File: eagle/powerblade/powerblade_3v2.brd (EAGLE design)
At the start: 25.4 x 25.4 mm, 80 parts, among them J1 JTAG_14PIN_IDC-ND, J2 AC_INF2, J4 TC2030-JLINK-NL, Q1 NTS4173, Q4 2SK1829, U1 TPS62122, U2 MCP6V3, U3 MSP430FR5738, U4 NRF51822QF, U6 MAX9910, U7 OPA2369, X1 16MHz, X3 32.768kHz, Y1 UREACH_XTEND

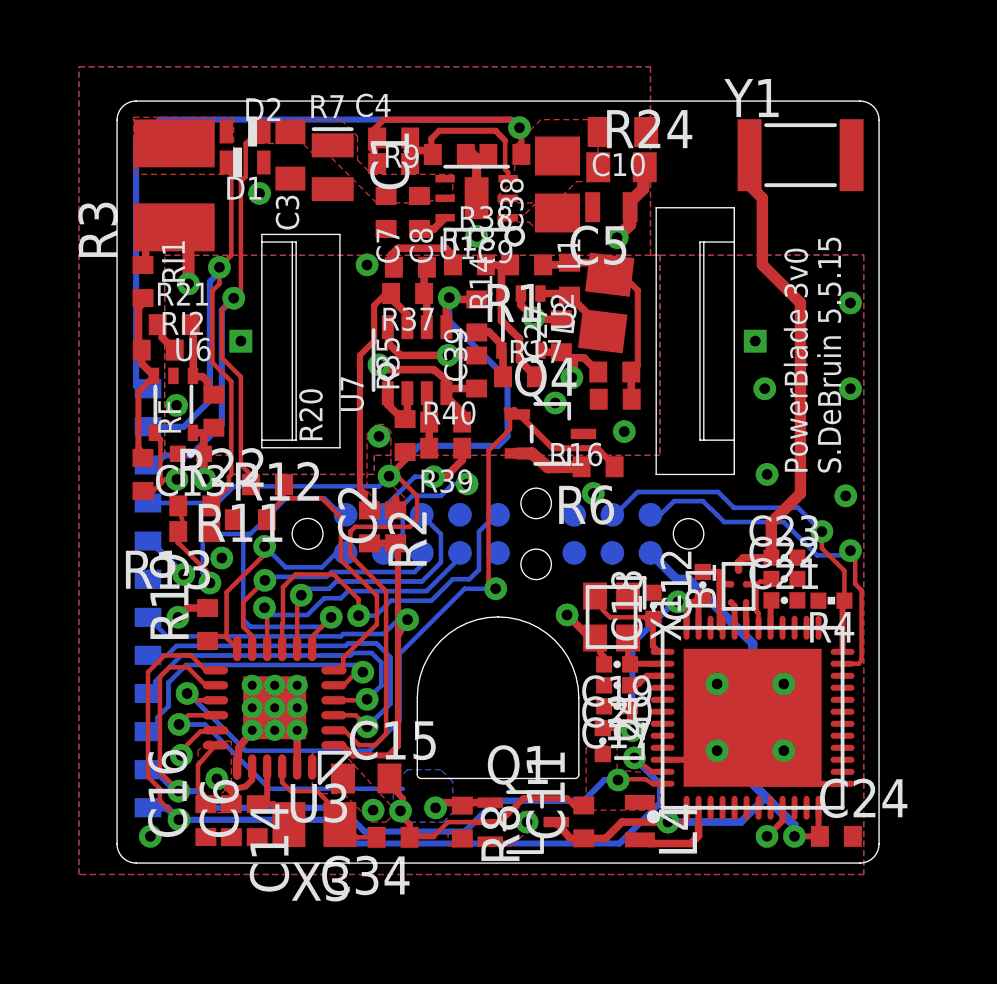
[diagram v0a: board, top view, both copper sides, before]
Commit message: updated powerblade 3v2 to include AC_F3
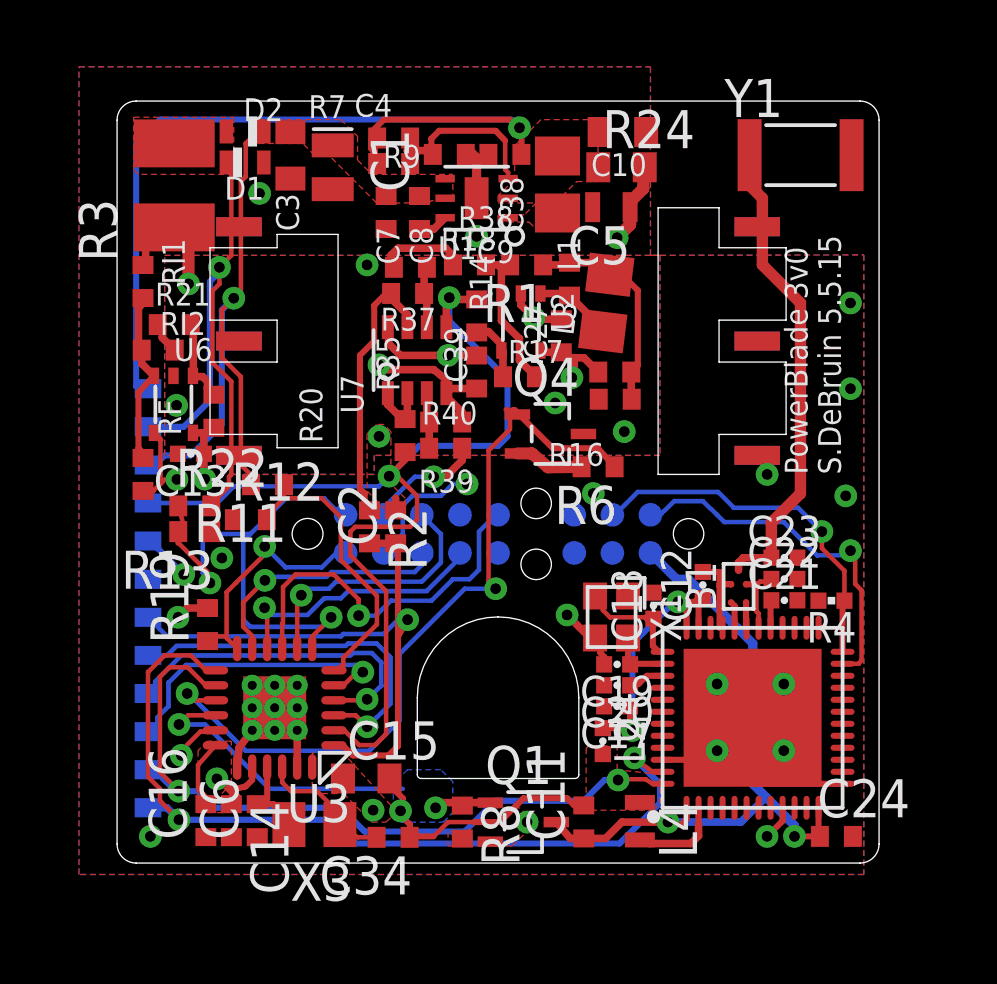
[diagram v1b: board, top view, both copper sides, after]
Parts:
- J2: value AC_INF2 -> AC_INF3; device powerfilm:AC3_F2 -> powerfilm:AC3_F3
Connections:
- net GND: now also J2.PB.1, J2.PB.2, J2.PB.3, J2.PB.4, J2.PB.5, J2.PB.6; no longer J2.P2A
- net VTEST: now also J2.PA.1, J2.PA.2, J2.PA.3, J2.PA.4, J2.PA.5, J2.PA.6; no longer J2.P1A
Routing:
- net VTEST: track 7.21 -> 10.4 mm
- net GND: vias 17 -> 16
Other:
- outline, holes or cut-outs redrawn
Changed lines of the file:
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@@
 <attribute name="DIGIKEY" value="490-4025-1-ND" x="4.727575" y="-16.002" size="1.778" layer="27" rot="R270" display="off"/>
 </element>
-<element name="J2" library="powerfilm" package="AC3_F2" value="AC_INF2" x="0" y="0">
+<element name="J2" library="powerfilm" package="AC3_F3" value="AC_INF3" x="0" y="0">
 <attribute name="DIGIKEY" value="NP" x="0" y="0" size="1.778" layer="27" display="off"/>
 </element>
@@
 <contactref element="RI1" pad="1"/>
 <contactref element="R3" pad="1"/>
-<contactref element="J2" pad="P1A"/>
+<contactref element="J2" pad="PA.1"/>
 <via x="-10.31875" y="1.905" extent="1-16" drill="0.3556"/>
 <wire x1="-10.31875" y1="1.905" x2="-10.31875" y2="3.314875" width="0.4064" layer="1"/>
@@
 <wire x1="-10.31875" y1="1.905" x2="-10.31875" y2="1.031875" width="1.27" layer="2"/>
 <wire x1="-10.31875" y1="1.031875" x2="-9.286875" y2="0" width="1.27" layer="2"/>
-<wire x1="-9.286875" y1="0" x2="-8.5725" y2="0" width="1.27" layer="2"/>
+<wire x1="-9.286875" y1="0" x2="-8.636" y2="3.81" width="1.27" layer="2"/>
 <wire x1="-11.8364" y1="2.534375" x2="-11.7475" y2="2.623275" width="0.254" layer="1"/>
 <wire x1="-11.7475" y1="2.623275" x2="-11.7475" y2="3.4925" width="0.254" layer="1"/>
 <wire x1="-11.7475" y1="3.4925" x2="-11.448875" y2="3.791125" width="0.254" layer="1"/>
 <wire x1="-11.448875" y1="3.791125" x2="-10.795" y2="3.791125" width="0.254" layer="1"/>
+<contactref element="J2" pad="PA.2"/>
+<contactref element="J2" pad="PA.3"/>
+<contactref element="J2" pad="PA.4"/>
+<contactref element="J2" pad="PA.5"/>
+<contactref element="J2" pad="PA.6"/>
+<wire x1="-8.636" y1="-3.81" x2="-8.636" y2="-3.81" width="0" layer="19" extent="1-16"/>
+<wire x1="-8.636" y1="0" x2="-8.636" y2="-3.81" width="0" layer="19" extent="1-1"/>
+<wire x1="-8.636" y1="0" x2="-8.636" y2="0" width="0" layer="19" extent="1-16"/>
+<wire x1="-9.286875" y1="0" x2="-8.636" y2="0" width="0" layer="19" extent="1-2"/>
+<wire x1="-8.636" y1="3.81" x2="-8.636" y2="3.81" width="0" layer="19" extent="1-2"/>
+<wire x1="-8.636" y1="3.81" x2="-8.636" y2="3.81" width="0" layer="19" extent="2-16"/>
 </signal>
 <signal name="VAMP">
@@
 <via x="-9.2075" y="-7.23138125" extent="1-16" drill="0.3556"/>
 <via x="-11.58875" y="-16.51" extent="1-16" drill="0.3556"/>
-<contactref element="J2" pad="P2A"/>
+<contactref element="J2" pad="PB.1"/>
 <wire x1="-3.81" y1="-7.0612" x2="-3.806825" y2="-7.0612" width="0.1524" layer="16"/>
 <wire x1="-3.806825" y1="-7.0612" x2="-3.175" y2="-6.429375" width="0.1524" layer="16"/>
@@
 <wire x1="-1.508125" y1="-4.7625" x2="-1.031875" y2="-4.7625" width="0.1524" layer="16"/>
 <contactref element="SV1" pad="P7"/>
-<via x="8.89" y="-1.5875" extent="1-16" drill="0.3556"/>
 <wire x1="-3.175" y1="-5.476875" x2="-2.8575" y2="-5.159375" width="0.1524" layer="16"/>
 <wire x1="-2.8575" y1="-5.159375" x2="-1.905" y2="-5.159375" width="0.1524" layer="16"/>
@@
 <wire x1="2.301875" y1="-15.24" x2="2.539275" y2="-15.4774" width="0.2032" layer="1"/>
 <wire x1="2.539275" y1="-15.4774" x2="2.8575" y2="-15.4774" width="0.2032" layer="1"/>
+<contactref element="J2" pad="PB.2"/>
+<contactref element="J2" pad="PB.3"/>
+<contactref element="J2" pad="PB.4"/>
+<contactref element="J2" pad="PB.5"/>
+<contactref element="J2" pad="PB.6"/>
+<wire x1="8.636" y1="3.81" x2="8.636" y2="3.81" width="0" layer="19" extent="1-16"/>
+<wire x1="8.636" y1="0" x2="8.636" y2="3.81" width="0" layer="19" extent="1-1"/>
+<wire x1="8.636" y1="0" x2="8.636" y2="0" width="0" layer="19" extent="1-16"/>
 </signal>
 </signals>

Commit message: fixed and approved some errors in powerblade 3v2
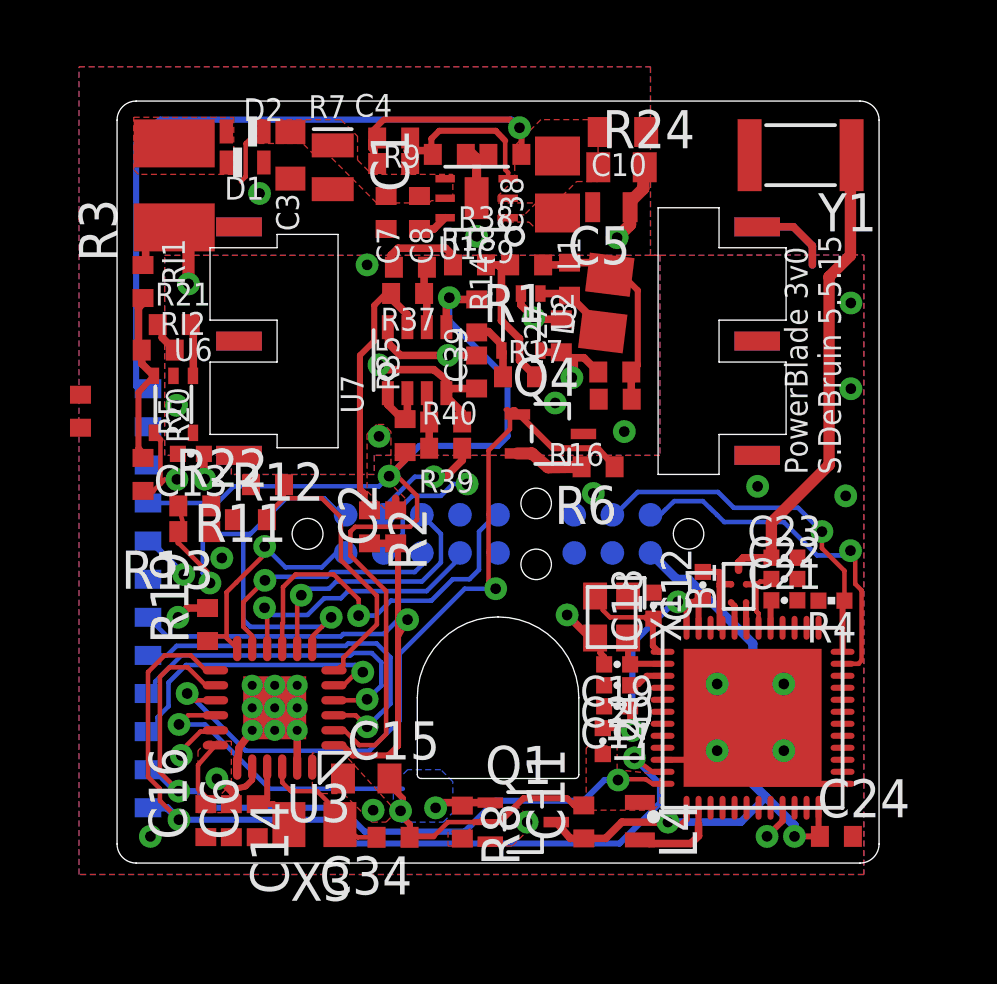
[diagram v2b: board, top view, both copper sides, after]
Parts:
- moved R20 4.45 mm to (-13.9, -2.34)
- turned Y1 to 180 degrees
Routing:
- net ZC: track 19.9 -> 0.66 mm, vias 1 -> 0
- net VCC: track 20.3 -> 2.38 mm, vias 1 -> 0
- net VTEST: track 10.4 -> 4.16 mm
- net GND: track 36.0 -> 41.5 mm
- net +3V3: track 20.8 -> 19.3 mm
- net N$40: track 2.85 -> 1.75 mm
